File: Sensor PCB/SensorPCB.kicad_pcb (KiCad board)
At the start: 2 copper layers, 16.3 x 18.5 mm, 4 parts, among them J1 Conn_01x05, U1 TSIC206-TO92

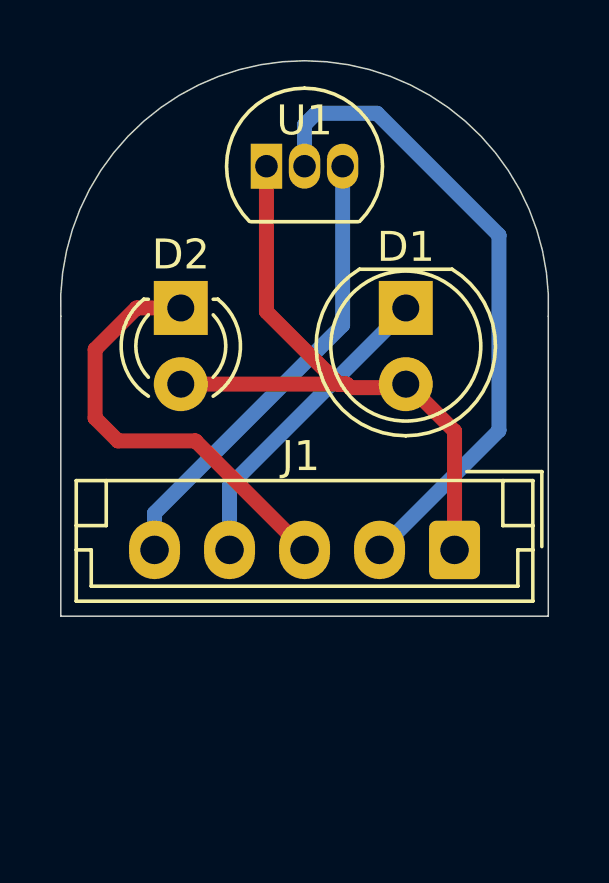
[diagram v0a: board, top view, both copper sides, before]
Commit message: Update PCB to have JST on Back side and add DRL Files
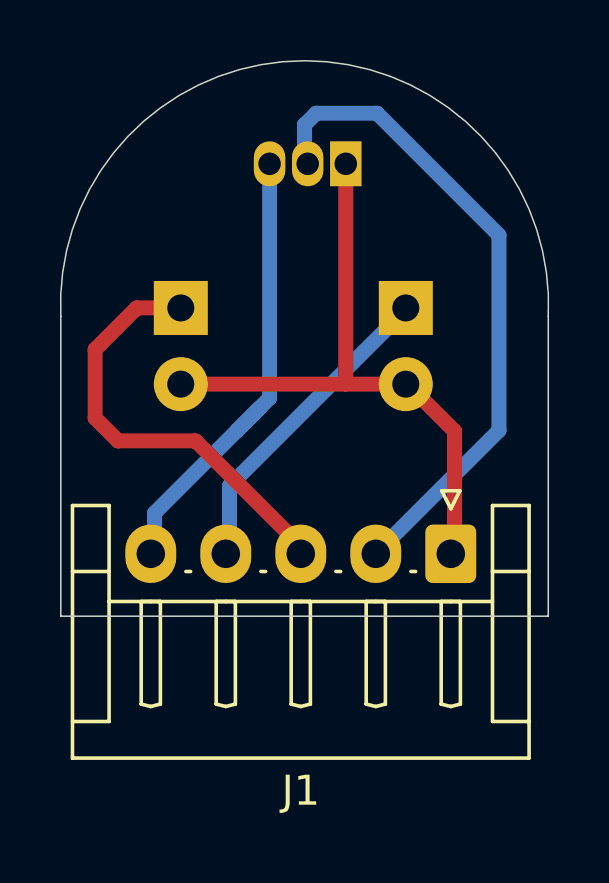
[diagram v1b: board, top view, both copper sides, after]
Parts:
- D1, D2, U1: moved to B.Cu
- J1: footprint Connector_JST:JST_EH_B5B-EH-A_1x05_P2.50mm_Vertical -> Connector_JST:JST_EH_S5B-EH_1x05_P2.50mm_Horizontal
- moved U1 2.65 mm to (144.5, 53.5), turned to 180 degrees
- moved J1 0.18 mm to (148.0, 66.5)
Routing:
- net Net-(D1-A): track 22.5 -> 21.0 mm
